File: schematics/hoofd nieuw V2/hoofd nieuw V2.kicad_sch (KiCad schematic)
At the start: 41 parts, among them J1 Conn_01x04_Pin, J2 Conn_01x02_Pin, J3 SFR02, J4 Conn_01x03_Pin, U1 ATtiny402-SS, U2 BH1750FVI-TR, U3 BH1750FVI-TR, Y1 ECS-2333MV-100-BN-TR

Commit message: zet alles op de juiste plaats
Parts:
- added H1, H2: MountingHole, MountingHole:MountingHole_3.5mm, symbol Mechanical:MountingHole
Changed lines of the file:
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@@
+	)
+	(symbol
+		(lib_id "Mechanical:MountingHole")
+		(at 39.37 160.02 0)
+		(unit 1)
+		(exclude_from_sim yes)
+		(in_bom no)
+		(on_board yes)
+		(dnp no)
+		(fields_autoplaced yes)
+		(property "Reference" "H2"
+			(at 41.91 158.7499 0)
+			(effects
+				(font
+					(size 1.27 1.27)
+				)
+				(justify left)
+			)
+		)
+		(property "Value" "MountingHole"
+			(at 41.91 161.2899 0)
+			(effects
+				(font
+					(size 1.27 1.27)
+				)
+				(justify left)
+			)
+		)
+		(property "Footprint" "MountingHole:MountingHole_3.5mm"
+			(at 39.37 160.02 0)
+			(effects
+				(font
+					(size 1.27 1.27)
+				)
+				(hide yes)
+			)
+		)
+		(property "Datasheet" "~"
+			(at 39.37 160.02 0)
+			(effects
+				(font
+					(size 1.27 1.27)
+				)
+				(hide yes)
+			)
+		)
+		(property "Description" "Mounting Hole without connection"
+			(at 39.37 160.02 0)
+			(effects
+				(font
+					(size 1.27 1.27)
+				)
+				(hide yes)
+			)
+		)
+		(instances
+			(project ""
+				(path "/7e0a6d27-e85c-4a07-8035-4491285a0fea"
+					(reference "H2")
+					(unit 1)
+				)
+			)
+		)
 	)
 	(symbol
@@
 					(unit 1)
 				)
+			)
+		)
+	)
+	(symbol
+		(lib_id "Mechanical:MountingHole")
+		(at 39.37 153.67 0)
+		(unit 1)
+		(exclude_from_sim yes)
+		(in_bom no)
+		(on_board yes)
+		(dnp no)
+		(fields_autoplaced yes)
+		(property "Reference" "H1"
+			(at 41.91 152.3999 0)
+			(effects
+				(font
+					(size 1.27 1.27)
+				)
+				(justify left)
+			)
+		)
+		(property "Value" "MountingHole"
+			(at 41.91 154.9399 0)
+			(effects
+				(font
+					(size 1.27 1.27)
+				)
+				(justify left)
+			)
+		)
+		(property "Footprint" "MountingHole:MountingHole_3.5mm"
+			(at 39.37 153.67 0)
+			(effects
+				(font
+					(size 1.27 1.27)
+				)
+				(hide yes)
+			)
+		)
+		(property "Datasheet" "~"
+			(at 39.37 153.67 0)
+			(effects
+				(font
+					(size 1.27 1.27)
+				)
+				(hide yes)
+			)
+		)
+		(property "Description" "Mounting Hole without connection"
+			(at 39.37 153.67 0)
+			(effects
+				(font
+					(size 1.27 1.27)
+				)
+				(hide yes)
+			)
+		)
+		(instances
+			(project ""
+				(path "/7e0a6d27-e85c-4a07-8035-4491285a0fea"
+					(reference "H1")
+					(unit 1)
+				)

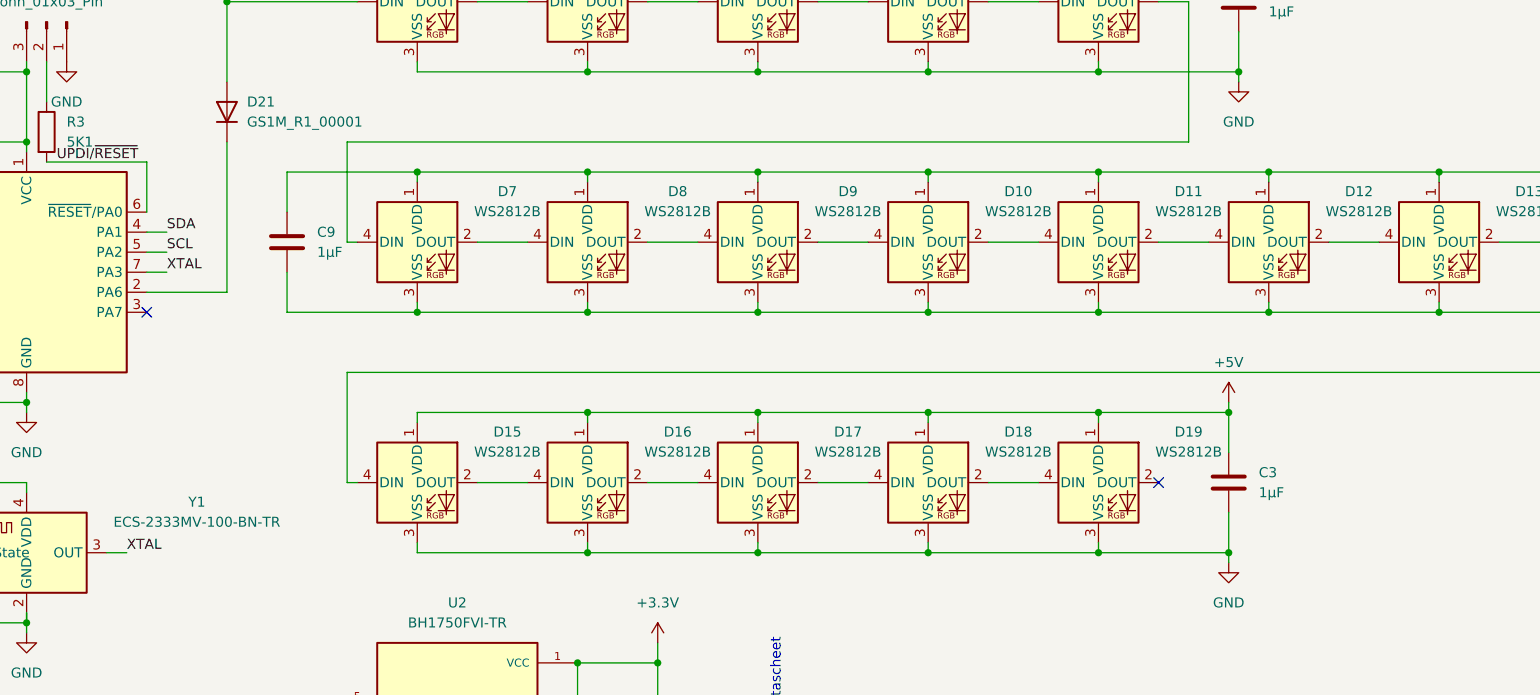
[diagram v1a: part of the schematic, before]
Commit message: teken al wat van het nieuw hoofd
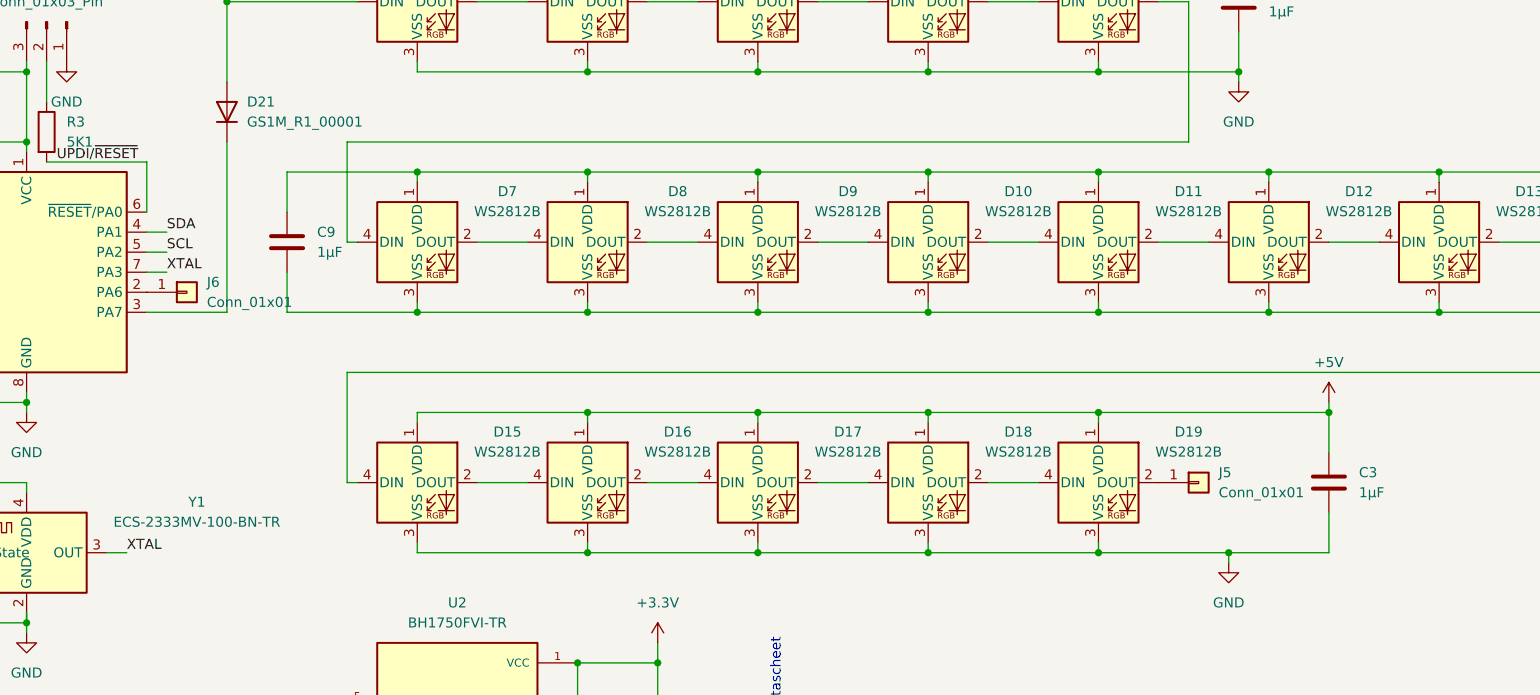
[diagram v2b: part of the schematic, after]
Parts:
- added J5, J6: Conn_01x01, Connector_Wire:SolderWirePad_1x01_SMD_1x2mm, symbol Connector_Generic:Conn_01x01
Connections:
- net at D21.1 (K): now also U1.3 (PA7); no longer U1.2 (PA6)
- net at D19.2 (DOUT): now also J5.1 (Pin_1)
- new net: J6.1 (Pin_1), U1.2 (PA6)
- no-connect marks 3 -> 1
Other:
- moved on the sheet: C3
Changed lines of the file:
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@@
 	)
 	(junction
-		(at 209.55 97.79)
+		(at 222.25 97.79)
 		(diameter 0)
 		(color 255 0 0 1)
@@
 	)
 	(no_connect
-		(at 200.66 106.68)
-	)
-	(no_connect
-		(at 72.39 85.09)
-	)
-	(no_connect
 		(at 85.09 33.02)
 	)
@@
 	(wire
 		(pts
-			(xy 193.04 97.79) (xy 209.55 97.79)
+			(xy 193.04 97.79) (xy 222.25 97.79)
 		)
 		(stroke
@@
 	(wire
 		(pts
-			(xy 209.55 110.49) (xy 209.55 115.57)
+			(xy 222.25 110.49) (xy 222.25 115.57)
 		)
 		(stroke
@@
 	(wire
 		(pts
-			(xy 82.55 63.5) (xy 82.55 82.55)
+			(xy 82.55 63.5) (xy 82.55 85.09)
 		)
 		(stroke
@@
 	(wire
 		(pts
-			(xy 209.55 97.79) (xy 209.55 102.87)
+			(xy 222.25 97.79) (xy 222.25 102.87)
 		)
 		(stroke
@@
 	(wire
 		(pts
+			(xy 72.39 85.09) (xy 82.55 85.09)
+		)
+		(stroke
+			(width 0)
+			(type default)
+		)
+	)
+	(wire
+		(pts
 			(xy 57.15 95.25) (xy 57.15 96.52)
 		)
@@
 	(wire
 		(pts
-			(xy 209.55 97.79) (xy 209.55 96.52)
+			(xy 222.25 97.79) (xy 222.25 96.52)
 		)
 		(stroke
@@
 	(wire
 		(pts
-			(xy 72.39 82.55) (xy 82.55 82.55)
-		)
-		(stroke
-			(width 0)
-			(type default)
-		)
-	)
-	(wire
-		(pts
 			(xy 50.8 54.61) (xy 57.15 54.61)
 		)
@@
 	(wire
 		(pts
+			(xy 222.25 115.57) (xy 209.55 115.57)
+		)
+		(stroke
+			(width 0)
+			(type default)
+		)
+	)
+	(wire
+		(pts
 			(xy 66.04 26.67) (xy 67.31 26.67)
 		)
@@
 	)
 	(symbol
+		(lib_id "Connector_Generic:Conn_01x01")
+		(at 205.74 106.68 0)
+		(unit 1)
+		(exclude_from_sim no)
+		(in_bom yes)
+		(on_board yes)
+		(dnp no)
+		(fields_autoplaced yes)
+		(property "Reference" "J5"
+			(at 208.28 105.4099 0)
+			(effects
+				(font
+					(size 1.27 1.27)
+				)
+				(justify left)
+			)
+		)
+		(property "Value" "Conn_01x01"
+			(at 208.28 107.9499 0)
+			(effects
+				(font
+					(size 1.27 1.27)
+				)
+				(justify left)
+			)
+		)
+		(property "Footprint" "Connector_Wire:SolderWirePad_1x01_SMD_1x2mm"
+			(at 205.74 106.68 0)
+			(effects
+				(font
+					(size 1.27 1.27)
+				)
+				(hide yes)
+			)
+		)
+		(property "Datasheet" "~"
+			(at 205.74 106.68 0)
+			(effects
+				(font
+					(size 1.27 1.27)
+				)
+				(hide yes)
+			)
+		)
+		(property "Description" "Generic connector, single row, 01x01, script generated (kicad-library-utils/schlib/autogen/connector/)"
+			(at 205.74 106.68 0)
+			(effects
+				(font
+					(size 1.27 1.27)
+				)
+				(hide yes)
+			)
+		)
+		(pin "1"
+		)
+		(instances
+			(project ""
+				(path "/7e0a6d27-e85c-4a07-8035-4491285a0fea"
+					(reference "J5")
+					(unit 1)
+				)
+			)
+		)
+	)
+	(symbol
 		(lib_id "robot:D5V0P4B5LP08")
 		(at 57.15 20.32 0)
@@
 	(symbol
 		(lib_id "Device:C")
-		(at 209.55 106.68 0)
+		(at 222.25 106.68 0)
 		(unit 1)
 		(exclude_from_sim no)
@@
 		(dnp no)
 		(property "Reference" "C3"
-			(at 213.36 105.4099 0)
+			(at 226.06 105.4099 0)
 			(effects
 				(font
@@
 		)
 		(property "Value" "1µF"
-			(at 213.36 107.95 0)
+			(at 226.06 107.95 0)
 			(effects
 				(font
@@
 		)
 		(property "Footprint" "Capacitor_SMD:C_0603_1608Metric"
-			(at 210.5152 110.49 0)
+			(at 223.2152 110.49 0)
 			(effects
 				(font
@@
 		)
 		(property "Datasheet" "~"
-			(at 209.55 106.68 0)
+			(at 222.25 106.68 0)
 			(effects
 				(font
@@
 		)
 		(property "Description" "Unpolarized capacitor"
-			(at 209.55 106.68 0)
+			(at 222.25 106.68 0)
 			(effects
 				(font
@@
 	(symbol
 		(lib_id "power:+5V")
-		(at 209.55 96.52 0)
+		(at 222.25 96.52 0)
 		(unit 1)
 		(exclude_from_sim no)
@@
 		(fields_autoplaced yes)
 		(property "Reference" "#PWR05"
-			(at 209.55 100.33 0)
+			(at 222.25 100.33 0)
 			(effects
 				(font
@@
 		)
 		(property "Value" "+5V"
-			(at 209.55 91.44 0)
+			(at 222.25 91.44 0)
 			(effects
 				(font
@@
 		)
 		(property "Footprint" ""
-			(at 209.55 96.52 0)
+			(at 222.25 96.52 0)
 			(effects
 				(font
@@
 		)
 		(property "Datasheet" ""
-			(at 209.55 96.52 0)
+			(at 222.25 96.52 0)
 			(effects
 				(font
@@
 		)
 		(property "Description" "Power symbol creates a global label with name \"+5V\""
-			(at 209.55 96.52 0)
+			(at 222.25 96.52 0)
 			(effects
 				(font
@@
 					(unit 1)
 				)
+			)
+		)
+	)
+	(symbol
+		(lib_id "Connector_Generic:Conn_01x01")
+		(at 77.47 82.55 0)
+		(unit 1)
+		(exclude_from_sim no)
+		(in_bom yes)
+		(on_board yes)
+		(dnp no)
+		(fields_autoplaced yes)
+		(property "Reference" "J6"
+			(at 80.01 81.2799 0)
+			(effects
+				(font
+					(size 1.27 1.27)
+				)
+				(justify left)
+			)
+		)
+		(property "Value" "Conn_01x01"
+			(at 80.01 83.8199 0)
+			(effects
+				(font
+					(size 1.27 1.27)
+				)
+				(justify left)
+			)
+		)
+		(property "Footprint" "Connector_Wire:SolderWirePad_1x01_SMD_1x2mm"
+			(at 77.47 82.55 0)
+			(effects
+				(font
+					(size 1.27 1.27)
+				)
+				(hide yes)
+			)
+		)
+		(property "Datasheet" "~"
+			(at 77.47 82.55 0)
+			(effects
+				(font
+					(size 1.27 1.27)
+				)
+				(hide yes)
+			)
+		)
+		(property "Description" "Generic connector, single row, 01x01, script generated (kicad-library-utils/schlib/autogen/connector/)"
+			(at 77.47 82.55 0)
+			(effects
+				(font
+					(size 1.27 1.27)
+				)
+				(hide yes)
+			)
+		)
+		(pin "1"
+		)
+		(instances
+			(project "hoofd nieuw V2"
+				(path "/7e0a6d27-e85c-4a07-8035-4491285a0fea"
+					(reference "J6")
+					(unit 1)
+				)

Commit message: nieuw hoofd V2 is klaar
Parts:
- removed D20: D5V0P4B5LP08, Library:D5V0P4B5LP08, symbol robot:D5V0P4B5LP08
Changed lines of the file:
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@@
-	)
-	(symbol
-		(lib_id "robot:D5V0P4B5LP08")
-		(at 57.15 20.32 0)
-		(unit 1)
-		(exclude_from_sim no)
-		(in_bom yes)
-		(on_board yes)
-		(dnp no)
-		(fields_autoplaced yes)
-		(property "Reference" "D20"
-			(at 59.69 17.78 0)
-			(effects
-				(font
-					(size 1.27 1.27)
-				)
-			)
-		)
-		(property "Value" "D5V0P4B5LP08"
-			(at 59.69 19.05 0)
-			(effects
-				(font
-					(size 1.27 1.27)
-				)
-			)
-		)
-		(property "Footprint" "Library:D5V0P4B5LP08"
-			(at 57.15 20.32 0)
-			(effects
-				(font
-					(size 1.27 1.27)
-				)
-				(hide yes)
-			)
-		)
-		(property "Datasheet" "https://www.diodes.com/assets/Datasheets/D5V0P4B5LP08.pdf"
-			(at 57.15 20.32 0)
-			(effects
-				(font
-					(size 1.27 1.27)
-				)
-				(hide yes)
-			)
-		)
-		(property "Description" ""
-			(at 57.15 20.32 0)
-			(effects
-				(font
-					(size 1.27 1.27)
-				)
-				(hide yes)
-			)
-		)
-		(pin "4"
-		)
-		(pin "1"
-		)
-		(pin "2"
-		)
-		(pin "3"
-		)
-		(pin "GND"
-		)
-		(instances
-			(project ""
-				(path "/7e0a6d27-e85c-4a07-8035-4491285a0fea"
-					(reference "D20")
-					(unit 1)
-				)
-			)
-		)
 	)
 	(symbol
